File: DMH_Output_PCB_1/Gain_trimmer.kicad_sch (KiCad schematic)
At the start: 8 parts, among them U8 TL074

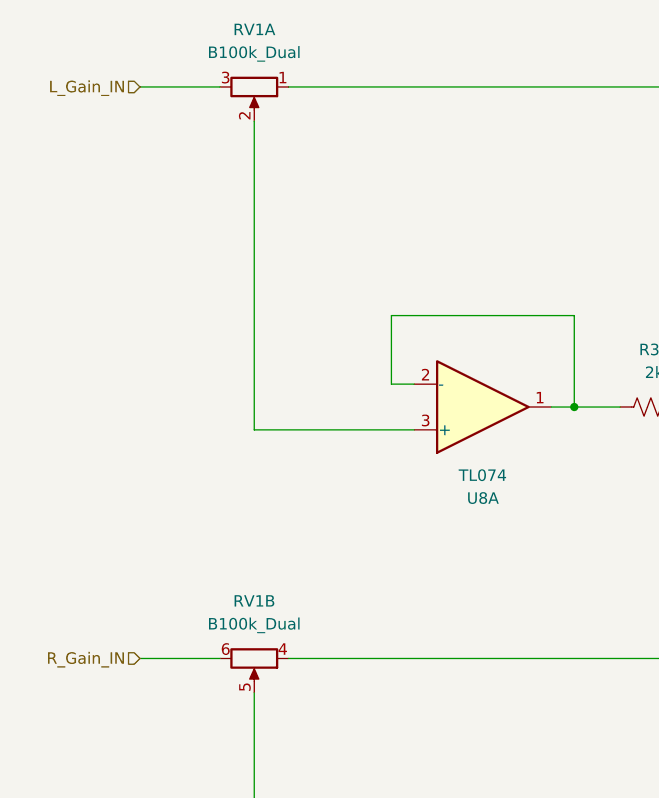
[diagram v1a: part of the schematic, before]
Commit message: Redesigned external input preamp
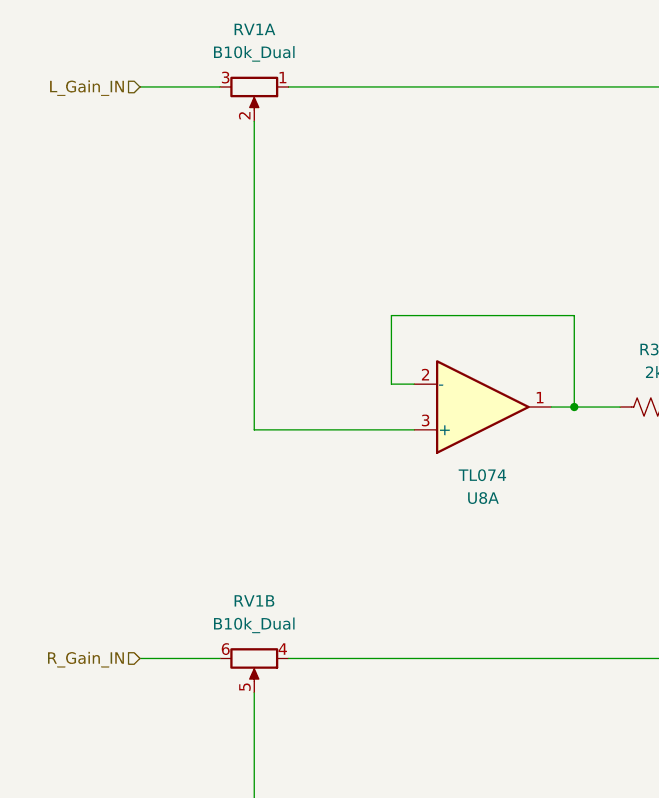
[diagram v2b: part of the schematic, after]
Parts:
- RV1: value B100k_Dual -> B10k_Dual
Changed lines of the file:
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@@
 			)
 		)
-		(property "Value" "B100k_Dual"
+		(property "Value" "B10k_Dual"
 			(at 76.2 46.99 90)
 			(effects
@@
 			)
 		)
-		(property "Value" "B100k_Dual"
+		(property "Value" "B10k_Dual"
 			(at 76.2 110.49 90)
 			(effects

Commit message: Adjusted gains
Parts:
- R30, R33: value 2k -> 1k
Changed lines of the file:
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@@
 			)
 		)
-		(property "Value" "2k"
+		(property "Value" "1k"
 			(at 120.65 146.05 90)
 			(effects
@@
 			)
 		)
-		(property "Value" "2k"
+		(property "Value" "1k"
 			(at 120.65 82.55 90)
 			(effects
@@
 			)
 		)
+		(property "Function" ""
+			(at 120.65 86.36 0)
+			(effects
+				(font
+					(size 1.27 1.27)
+				)
+			)
+		)

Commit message: Adjustments during breadboarding
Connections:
- net GND: now also U8.5 (+); no longer U8.12 (+)
- net L_Gain_OUT: now also U8.7; no longer U8.14
- net at RV1.5: now also U8.12 (+); no longer U8.5 (+)
- net at C11.1, R30.2, R31.1: now also U8.6 (-); no longer U8.13 (-)
- new net: R33.1, U8.13 (-), U8.14
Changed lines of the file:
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@@
 		(at 101.6 149.86 0)
 		(mirror x)
-		(unit 2)
+		(unit 4)
 		(exclude_from_sim no)
 		(in_bom yes)
@@
 			)
 		)
+		(property "Function" ""
+			(at 101.6 149.86 0)
+			(effects
+				(font
+					(size 1.27 1.27)
+				)
+			)
+		)
 		(pin "7"
 		)
@@
 				(path "/58f4306d-5387-4983-bb08-41a2313fd315/9adc9203-60fe-4942-b6ff-2cd29597aa58"
 					(reference "U8")
-					(unit 2)
+					(unit 4)
 				)
 			)
@@
 			)
 		)
+		(property "Function" ""
+			(at 139.7 152.4 0)
+			(effects
+				(font
+					(size 1.27 1.27)
+				)
+			)
+		)
 		(pin "7"
 		)
@@
 			)
 		)
+		(property "Function" ""
+			(at 101.6 86.36 0)
+			(effects
+				(font
+					(size 1.27 1.27)
+				)
+			)
+		)
 		(pin "7"
 		)
@@
 		(at 139.7 88.9 0)
 		(mirror x)
-		(unit 4)
+		(unit 2)
 		(exclude_from_sim no)
 		(in_bom yes)
@@
 			)
 		)
+		(property "Function" ""
+			(at 139.7 88.9 0)
+			(effects
+				(font
+					(size 1.27 1.27)
+				)
+			)
+		)
 		(pin "7"
 		)
@@
 				(path "/58f4306d-5387-4983-bb08-41a2313fd315/9adc9203-60fe-4942-b6ff-2cd29597aa58"
 					(reference "U8")
-					(unit 4)
-				)
-			)
+					(unit 2)
+				)
+			)
